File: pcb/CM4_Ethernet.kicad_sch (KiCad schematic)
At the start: 17 parts, among them U1 74LVC1G07SE-7, U1 TPD4EUSB30, U2 TPD4EUSB30, U3 MagJack-A70-112-331N126

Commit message: - ERC checks
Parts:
- Module1: footprint Footprints:Raspberry-Pi-4-Compute-Module -> CM4IO:Raspberry-Pi-4-Compute-Module; Field5 2off DF40C-100DS-0.4V -> 2x DF40C-100DS-0.4V
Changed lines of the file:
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@@
     (stroke (width 0) (type solid))
+  )
+  (wire (pts (xy 212.09 57.15) (xy 212.09 55.88))
+    (stroke (width 0) (type default))
   )
   (bus (pts (xy 147.32 57.15) (xy 147.32 87.63))
@@
     (effects (font (size 1.27 1.27)) (justify right bottom))
   )
-  (label "AC.~{ENABLE}" (at 24.13 85.09 0)
+  (label "AC.~{ENABLE}" (at 24.13 85.09 0) (fields_autoplaced)
     (effects (font (size 1.27 1.27)) (justify left bottom))
   )
@@
     (effects (font (size 1.27 1.27)) (justify right bottom))
   )
-  (label "I2S.LRCK" (at 20.32 59.69 0)
+  (label "I2S.LRCK" (at 20.32 59.69 0) (fields_autoplaced)
     (effects (font (size 1.27 1.27)) (justify left bottom))
   )
@@
     (effects (font (size 1.27 1.27)) (justify right bottom))
   )
-  (label "I2S.D" (at 138.43 59.69 0)
+  (label "I2S.D" (at 138.43 59.69 0) (fields_autoplaced)
     (effects (font (size 1.27 1.27)) (justify left bottom))
   )
-  (label "AC.~{MUTE}" (at 24.13 82.55 0)
+  (label "AC.~{MUTE}" (at 24.13 82.55 0) (fields_autoplaced)
     (effects (font (size 1.27 1.27)) (justify left bottom))
   )
@@
     (effects (font (size 1.27 1.27)) (justify right bottom))
   )
-  (label "I2S.BCK" (at 138.43 90.17 0)
+  (label "I2S.BCK" (at 138.43 90.17 0) (fields_autoplaced)
     (effects (font (size 1.27 1.27)) (justify left bottom))
   )
@@
     (effects (font (size 1.27 1.27)) (justify right bottom))
   )
-  (label "AC.~{ERROR}" (at 24.13 90.17 0)
+  (label "AC.~{ERROR}" (at 24.13 90.17 0) (fields_autoplaced)
     (effects (font (size 1.27 1.27)) (justify left bottom))
   )
@@
     (effects (font (size 1.27 1.27)) (justify right bottom))
   )
-  (label "AC.~{CLIP}" (at 24.13 87.63 0)
+  (label "AC.~{CLIP}" (at 24.13 87.63 0) (fields_autoplaced)
     (effects (font (size 1.27 1.27)) (justify left bottom))
   )
@@
     )
   )
-  (symbol (lib_id "Device:LED") (at 165.1 129.54 90) (unit 1)
+  (symbol (lib_name "LED_1") (lib_id "Device:LED") (at 165.1 129.54 90) (unit 1)
     (in_bom yes) (on_board yes) (dnp no)
     (property "Reference" "D2" (at 168.0718 128.5494 90)
@@
       (effects (font (size 1.27 1.27)) hide)
     )
-    (property "Datasheet" "http://optoelectronics.liteon.com/upload/download/DS22-2000-210/LTST-S270KRKT.pdf" (at 165.1 129.54 0)
+    (property "Datasheet" "~" (at 165.1 129.54 0)
       (effects (font (size 1.27 1.27)) hide)
     )
@@
     )
   )
-  (symbol (lib_id "power:GND") (at 229.87 100.33 0) (unit 1)
+  (symbol (lib_name "GND_3") (lib_id "power:GND") (at 229.87 100.33 0) (unit 1)
     (in_bom yes) (on_board yes) (dnp no)
     (property "Reference" "#PWR04" (at 229.87 106.68 0)
@@
     )
   )
-  (symbol (lib_id "power:GND") (at 190.5 53.34 0) (unit 1)
+  (symbol (lib_name "GND_6") (lib_id "power:GND") (at 190.5 53.34 0) (unit 1)
     (in_bom yes) (on_board yes) (dnp no)
     (property "Reference" "#PWR01" (at 190.5 59.69 0)
@@
       (effects (font (size 1.27 1.27)) hide)
     )
-    (property "Datasheet" "http://optoelectronics.liteon.com/upload/download/DS22-2000-226/LTST-S270KGKT.pdf" (at 129.54 35.56 0)
+    (property "Datasheet" "~" (at 129.54 35.56 0)
       (effects (font (size 1.27 1.27)) hide)
     )
@@
     )
   )
-  (symbol (lib_id "power:GND") (at 190.5 85.09 0) (unit 1)
+  (symbol (lib_name "GND_5") (lib_id "power:GND") (at 190.5 85.09 0) (unit 1)
     (in_bom yes) (on_board yes) (dnp no)
     (property "Reference" "#PWR02" (at 190.5 91.44 0)
@@
       (effects (font (size 1.27 1.27)))
     )
-    (property "Footprint" "Footprints:Raspberry-Pi-4-Compute-Module" (at 227.33 111.76 0)
+    (property "Footprint" "CM4IO:Raspberry-Pi-4-Compute-Module" (at 227.33 111.76 0)
       (effects (font (size 1.27 1.27)) hide)
     )
@@
       (effects (font (size 1.27 1.27)) hide)
     )
-    (property "Field5" "2off DF40C-100DS-0.4V" (at 85.09 85.09 0)
+    (property "Field5" "2x DF40C-100DS-0.4V" (at 85.09 85.09 0)
       (effects (font (size 1.27 1.27)) hide)
     )
@@
     )
   )
-  (symbol (lib_id "power:GND") (at 50.8 158.75 0) (unit 1)
+  (symbol (lib_name "GND_1") (lib_id "power:GND") (at 50.8 158.75 0) (unit 1)
     (in_bom yes) (on_board yes) (dnp no)
     (property "Reference" "#PWR04" (at 50.8 165.1 0)
@@
     )
   )
-  (symbol (lib_id "power:GND") (at 114.3 158.75 0) (unit 1)
+  (symbol (lib_name "GND_2") (lib_id "power:GND") (at 114.3 158.75 0) (unit 1)
     (in_bom yes) (on_board yes) (dnp no)
     (property "Reference" "#PWR05" (at 114.3 165.1 0)
@@
     )
   )
-  (symbol (lib_id "power:GND") (at 212.09 55.88 0) (unit 1)
-    (in_bom yes) (on_board yes) (dnp no)
-    (property "Reference" "#PWR03" (at 212.09 62.23 0)
-      (effects (font (size 1.27 1.27)) hide)
-    )
-    (property "Value" "GND" (at 212.217 60.2742 0)
-      (effects (font (size 1.27 1.27)))
-    )
-    (property "Footprint" "" (at 212.09 55.88 0)
-      (effects (font (size 1.27 1.27)) hide)
-    )
-    (property "Datasheet" "" (at 212.09 55.88 0)
-      (effects (font (size 1.27 1.27)) hide)
-    )
+  (symbol (lib_name "GND_4") (lib_id "power:GND") (at 212.09 57.15 0) (unit 1)
+    (in_bom yes) (on_board yes) (dnp no)
+    (property "Reference" "#PWR03" (at 212.09 63.5 0)
+      (effects (font (size 1.27 1.27)) hide)
+    )
+    (property "Value" "GND" (at 212.217 61.5442 0)
+      (effects (font (size 1.27 1.27)))
+    )
+    (property "Footprint" "" (at 212.09 57.15 0)
+      (effects (font (size 1.27 1.27)) hide)
+    )
+    (property "Datasheet" "" (at 212.09 57.15 0)
+      (effects (font (size 1.27 1.27)) hide)
+    )

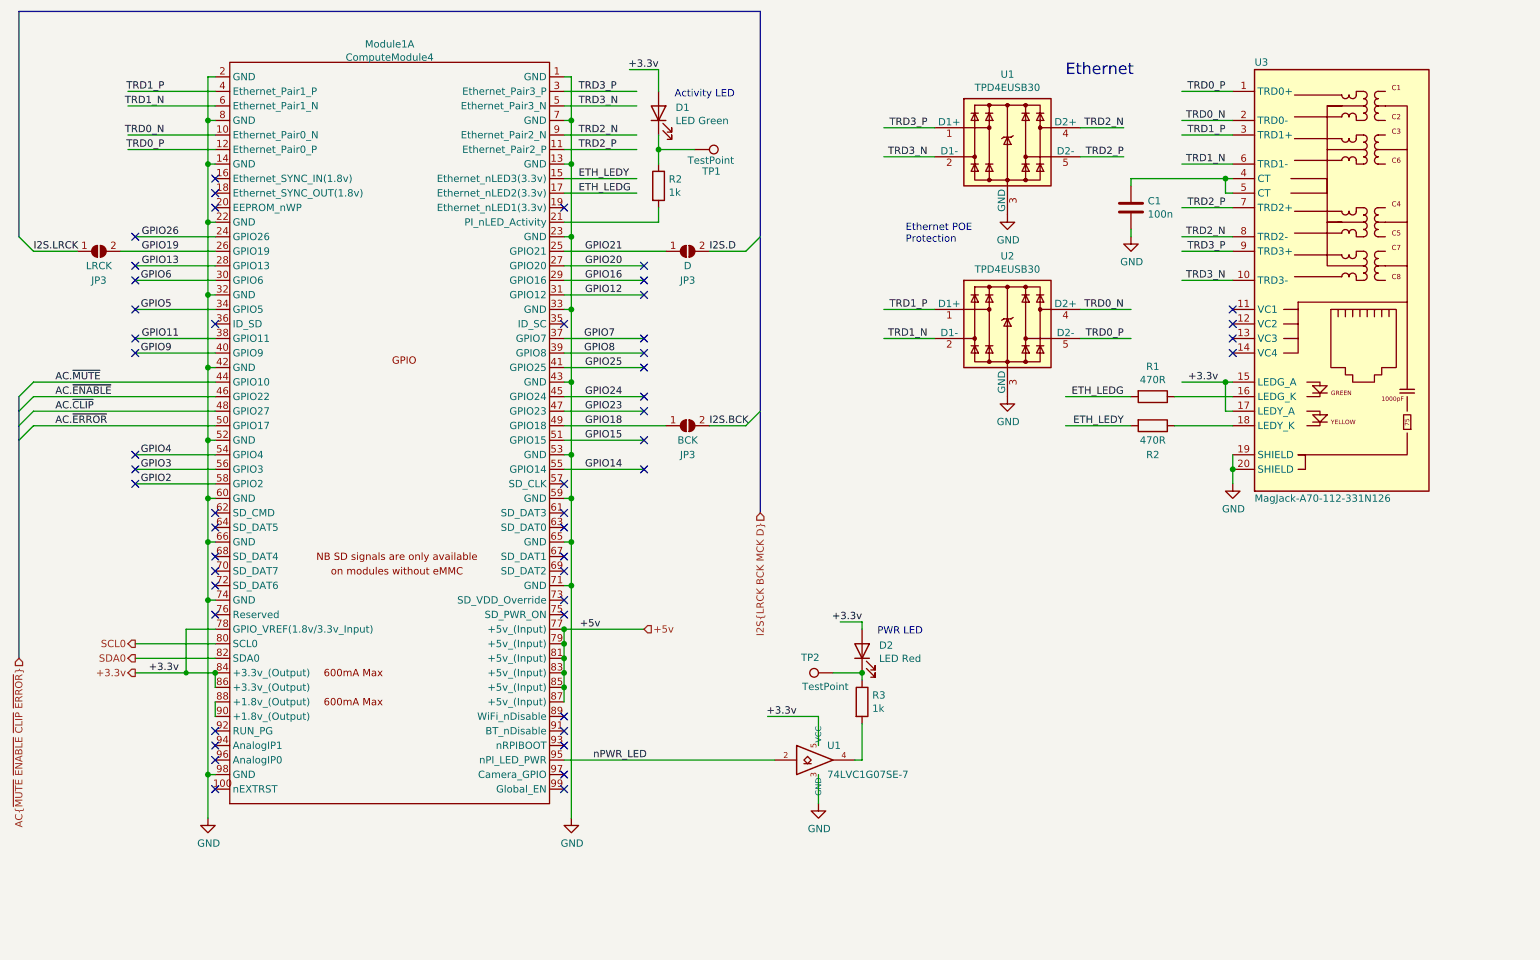
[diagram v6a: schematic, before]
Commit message: - work in progress, changed rj45 connector
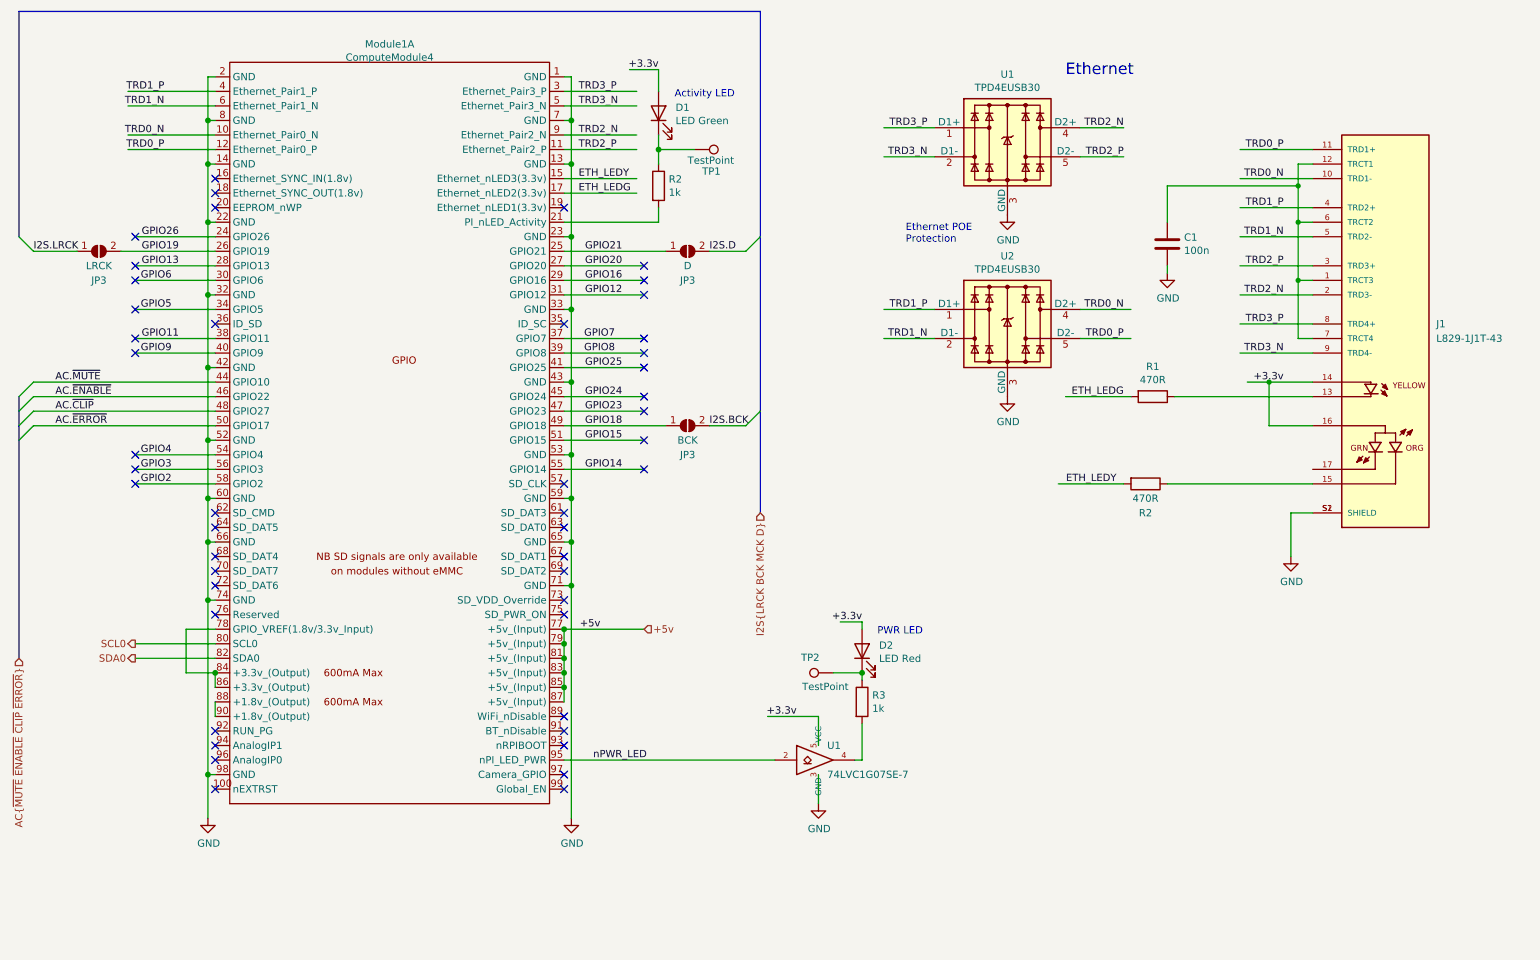
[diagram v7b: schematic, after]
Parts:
- removed U3: MagJack-A70-112-331N126, Footprints:TRJG0926HENL, symbol CM4IO:MagJack-A70-112-331N126
- added J1: L829-1J1T-43, Footprints:BEL_L829-1J1T-43, symbol L829-1J1T-43:L829-1J1T-43
- Module1: footprint CM4IO:Raspberry-Pi-4-Compute-Module -> Footprints:Raspberry-Pi-4-Compute-Module
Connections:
- net +3.3v: now also J1.14, J1.16; no longer Module1.78 (GPIO_VREF(1.8v/3.3v_Input)), Module1.84 (+3.3v_(Output)), Module1.86 (+3.3v_(Output))
- net GND: now also J1.S1 (SHIELD), J1.S2 (SHIELD)
- net TRD0_N: now also J1.10 (TRD1-)
- net TRD0_P: now also J1.11 (TRD1+)
- net TRD1_N: now also J1.5 (TRD2-)
- net TRD1_P: now also J1.4 (TRD2+)
- net TRD2_N: now also J1.2 (TRD3-)
- net TRD2_P: now also J1.3 (TRD3+)
- net TRD3_N: now also J1.9 (TRD4-)
- net TRD3_P: now also J1.8 (TRD4+)
- net at R2.1: now also J1.15
- net at R1.1: now also J1.13
- net at C1.1: now also J1.1 (TRCT3), J1.12 (TRCT1), J1.6 (TRCT2), J1.7 (TRCT4)
- new net: Module1.78 (GPIO_VREF(1.8v/3.3v_Input)), Module1.84 (+3.3v_(Output)), Module1.86 (+3.3v_(Output))
- no-connect marks 51 -> 47
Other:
- moved on the sheet: C1, R2

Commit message: - placing components
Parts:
- added R1: 470R, Resistor_SMD:R_0805_2012Metric_Pad1.20x1.40mm_HandSolder, symbol Device:R
- J1: Farnell (none) -> 2675997
- Module1: Farnell (none) -> 2427679
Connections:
- net at J1.17: now also R1.1
- net at Module1.19 (Ethernet_nLED1(3.3v)): now also R1.2
- no-connect marks 47 -> 46
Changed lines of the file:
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@@
   (no_connect (at 52.07 46.99))
   (no_connect (at 52.07 123.19))
-  (no_connect (at 113.03 52.07))
   (no_connect (at 113.03 100.33))
   (no_connect (at 38.1 64.77))
@@
     (stroke (width 0) (type solid))
   )
+  (wire (pts (xy 226.06 97.79) (xy 226.06 93.98))
+    (stroke (width 0) (type default))
+  )
   (wire (pts (xy 113.03 31.75) (xy 125.73 31.75))
     (stroke (width 0) (type solid))
@@
     (stroke (width 0) (type solid))
   )
+  (wire (pts (xy 116.84 53.34) (xy 116.84 52.07))
+    (stroke (width 0) (type default))
+  )
   (wire (pts (xy 243.84 44.45) (xy 241.3 44.45))
     (stroke (width 0) (type default))
@@
     (stroke (width 0) (type solid))
   )
+  (wire (pts (xy 152.4 53.34) (xy 116.84 53.34))
+    (stroke (width 0) (type default))
+  )
   (wire (pts (xy 231.14 57.15) (xy 243.84 57.15))
     (stroke (width 0) (type solid))
@@
     (stroke (width 0) (type solid))
   )
+  (wire (pts (xy 116.84 52.07) (xy 113.03 52.07))
+    (stroke (width 0) (type default))
+  )
   (wire (pts (xy 241.3 64.77) (xy 241.3 74.93))
     (stroke (width 0) (type default))
@@
     (stroke (width 0) (type solid))
   )
+  (wire (pts (xy 243.84 97.79) (xy 226.06 97.79))
+    (stroke (width 0) (type default))
+  )
   (wire (pts (xy 20.32 90.17) (xy 52.07 90.17))
     (stroke (width 0) (type default))
@@
     (stroke (width 0) (type solid))
   )
+  (wire (pts (xy 152.4 93.98) (xy 152.4 53.34))
+    (stroke (width 0) (type default))
+  )
   (wire (pts (xy 38.1 69.85) (xy 52.07 69.85))
     (stroke (width 0) (type solid))
@@
     (stroke (width 0) (type solid))
   )
+  (wire (pts (xy 226.06 93.98) (xy 218.44 93.98))
+    (stroke (width 0) (type default))
+  )
   (wire (pts (xy 113.03 57.15) (xy 114.3 57.15))
     (stroke (width 0) (type solid))
@@
     (stroke (width 0) (type default))
   )
-  (wire (pts (xy 129.54 54.61) (xy 129.54 52.07))
+  (wire (pts (xy 129.54 52.07) (xy 129.54 54.61))
     (stroke (width 0) (type solid))
   )
@@
   )
   (wire (pts (xy 241.3 54.61) (xy 241.3 64.77))
+    (stroke (width 0) (type default))
+  )
+  (wire (pts (xy 210.82 93.98) (xy 152.4 93.98))
     (stroke (width 0) (type default))
   )
@@
     (property "MANUFACTURER" "Bel Fuse" (at 256.54 72.39 0)
       (effects (font (size 1.27 1.27)) (justify bottom) hide)
+    )
+    (property "Farnell" "2675997" (at 256.54 72.39 0)
+      (effects (font (size 1.27 1.27)) hide)
     )
     (pin "12")
@@
     )
   )
+  (symbol (lib_id "Device:R") (at 214.63 93.98 270) (unit 1)
+    (in_bom yes) (on_board yes) (dnp no)
+    (property "Reference" "R1" (at 214.63 88.7222 90)
+      (effects (font (size 1.27 1.27)))
+    )
+    (property "Value" "470R" (at 214.63 91.0336 90)
+      (effects (font (size 1.27 1.27)))
+    )
+    (property "Footprint" "Resistor_SMD:R_0805_2012Metric_Pad1.20x1.40mm_HandSolder" (at 214.63 92.202 90)
+      (effects (font (size 1.27 1.27)) hide)
+    )
+    (property "Datasheet" "https://fscdn.rohm.com/en/products/databook/datasheet/passive/resistor/chip_resistor/mcr-e.pdf" (at 214.63 93.98 0)
+      (effects (font (size 1.27 1.27)) hide)
+    )
+    (property "Field4" "Farnell" (at 214.63 93.98 0)
+      (effects (font (size 1.27 1.27)) hide)
+    )
+    (property "Field5" "9239197" (at 214.63 93.98 0)
+      (effects (font (size 1.27 1.27)) hide)
+    )
+    (property "Field7" "KOA EUROPE GMBH" (at 214.63 93.98 0)
+      (effects (font (size 1.27 1.27)) hide)
+    )
+    (property "Field6" "RK73G1ETQTP4700D         " (at 214.63 93.98 0)
+      (effects (font (size 1.27 1.27)) hide)
+    )
+    (property "Field8" "120887981" (at 214.63 93.98 0)
+      (effects (font (size 1.27 1.27)) hide)
+    )
+    (property "Part Description" "Resistor 470R M1005 1% 63mW" (at 214.63 93.98 0)
+      (effects (font (size 1.27 1.27)) hide)
+    )
+    (pin "1")
+    (pin "2")
+    (instances
+      (project "VolumioAmp"
+        (path "/c639bae0-d26f-43ee-9e8c-ca060284bd0b/714de229-102b-48b6-a22b-2290164179cf"
+          (reference "R1") (unit 1)
+        )
+        (path "/c639bae0-d26f-43ee-9e8c-ca060284bd0b/0d83f7c4-6343-47e0-83de-c41ded3b9d5e"
+          (reference "R24") (unit 1)
+        )
+      )
+      (project "CM4IOv5"
+        (path "/e63e39d7-6ac0-4ffd-8aa3-1841a4541b55/00000000-0000-0000-0000-00005cff706a"
+          (reference "R2") (unit 1)
+        )
+      )
+    )
+  )
   (symbol (lib_id "CM4IO:ComputeModule4-CM4") (at 85.09 85.09 0) (unit 1)
     (in_bom yes) (on_board yes) (dnp no)
@@
       (effects (font (size 1.27 1.27)) hide)
     )
+    (property "Farnell" "2427679" (at 85.09 85.09 0)
+      (effects (font (size 1.27 1.27)) hide)
+    )
